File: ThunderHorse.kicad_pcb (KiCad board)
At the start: 6 copper layers, 99.1 x 60 mm, 260 parts, among them J1 JTAG, J10 MOTOR1, J11 SWD1, J12 MOTOR1, J13 SWD1, J14 MOTOR1, J16 UFL, J17 IO1, J18 IO2, J2 HH-16P-CB-TYPE-C, J3 GPS, J4 CAM, J5 GPS, J6 CAM, J7 SWD1, J8 MOTOR1, J9 SWD1, Q1 XRS306D, Q10 XRS306D, Q11 XRS306D, Q12 XRS306D, Q13 SI2312BDS, Q2 XRS306D, Q3 XRS306D, Q4 XRS306D, Q5 XRS306D, Q6 XRS306D, Q7 XRS306D, Q8 XRS306D, Q9 XRS306D, SW1 TS2306A, SW2 TS2306A, U1 BATTERY, U10 STM32G071GBUxN, U11 DRV8300D, U12 STM32G071GBUxN, U13 DRV8300D, U14 STM32G071GBUxN, U15 DRV8300D, U16 TPRT9013-33, U17 ICM-42688-P, U18 BMP280, U19 INA230, U2 TPS63070RNMR, U20 TPRT9013-33, U21 SX1280IMLTRT, U22 AT2401C, U3 TPRT9013-33, U4 TPS2121, U5 RP2354B, U6 W25Q128JVPIQ, U7 USBLC6-2P6, U8 STM32G071GBUxN, U9 DRV8300D, Y1 40MHz, Y2 52MHz/10ppm

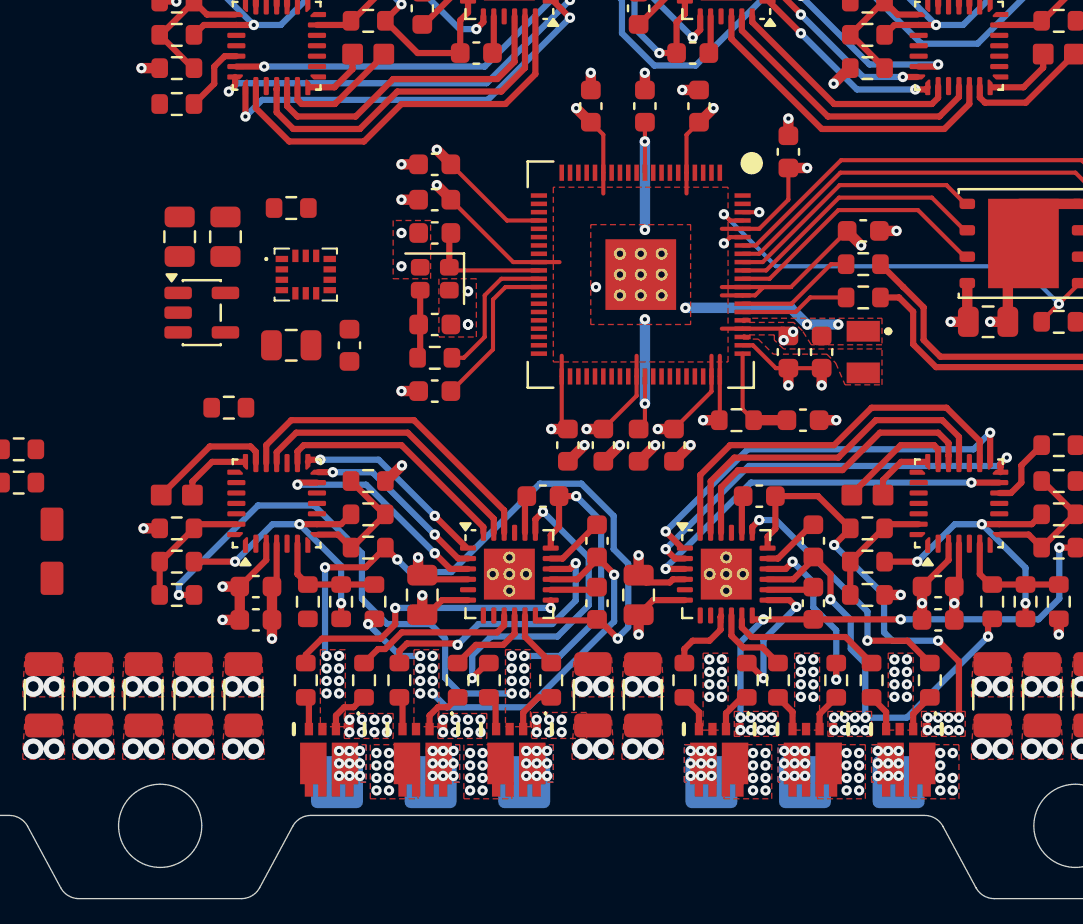
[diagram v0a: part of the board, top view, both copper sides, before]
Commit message: IMU layout
Completed the IMU layout.

TODO:
Continue with the transceiver routing.
Connect each ESC to the MCU.
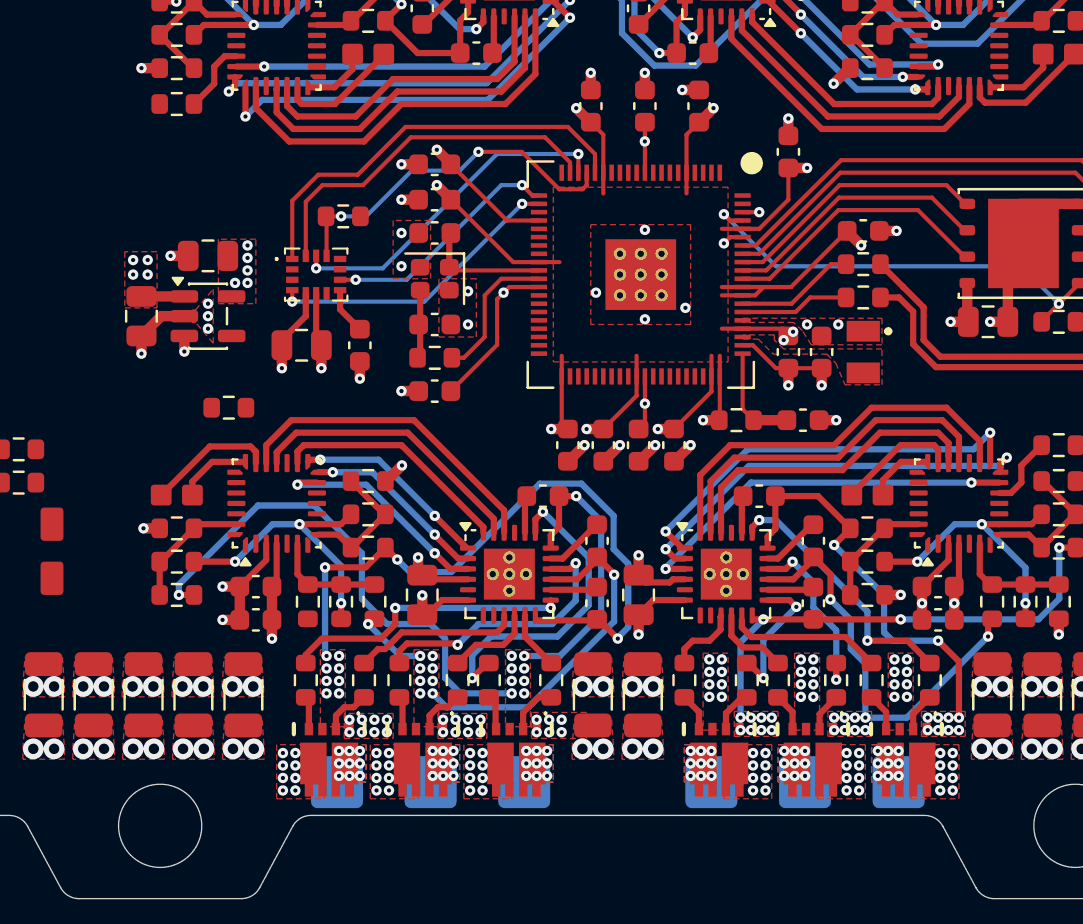
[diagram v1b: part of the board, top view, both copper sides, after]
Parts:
- moved C86 4.24 mm to (117.1, 102.0), turned to -90 degrees
- moved R83 2.53 mm to (126.8, 97.2), turned to 180 degrees
- moved C87 1.24 mm to (120.3, 99.1), turned to 180 degrees
- moved C84 0.50 mm to (124.8, 103.4)
- moved C85 0.50 mm to (127.6, 103.4)
- moved U17 0.50 mm to (125.5, 100.0)
- moved U16 0.34 mm to (120.3, 102.0)
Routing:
- net IMU_MISO: track 0.00 -> 20.3 mm
- net IMU_MOSI: track 0.00 -> 17.6 mm
- net IMU_CS: track 0.00 -> 17.2 mm, vias 0 -> 2
- net IMU_SCLK: track 0.00 -> 16.4 mm, vias 0 -> 2
- net IMU_INT: track 0.00 -> 14.4 mm, vias 0 -> 2
- net IMU_CLK: track 0.00 -> 11.6 mm, vias 0 -> 2
- net GND: track 85.6 -> 94.2 mm, vias 237 -> 243
- net 3V3_IMU: track 0.00 -> 6.34 mm, vias 0 -> 6
- net 1V1: track 29.0 -> 33.3 mm, vias 8 -> 9
- net 5V: track 17.4 -> 20.3 mm, vias 19 -> 24
- net VBAT: vias 160 -> 169
- added copper zone on F.Cu, net 3V3_IMU
- added copper zone on In2.Cu, net 3V3_IMU

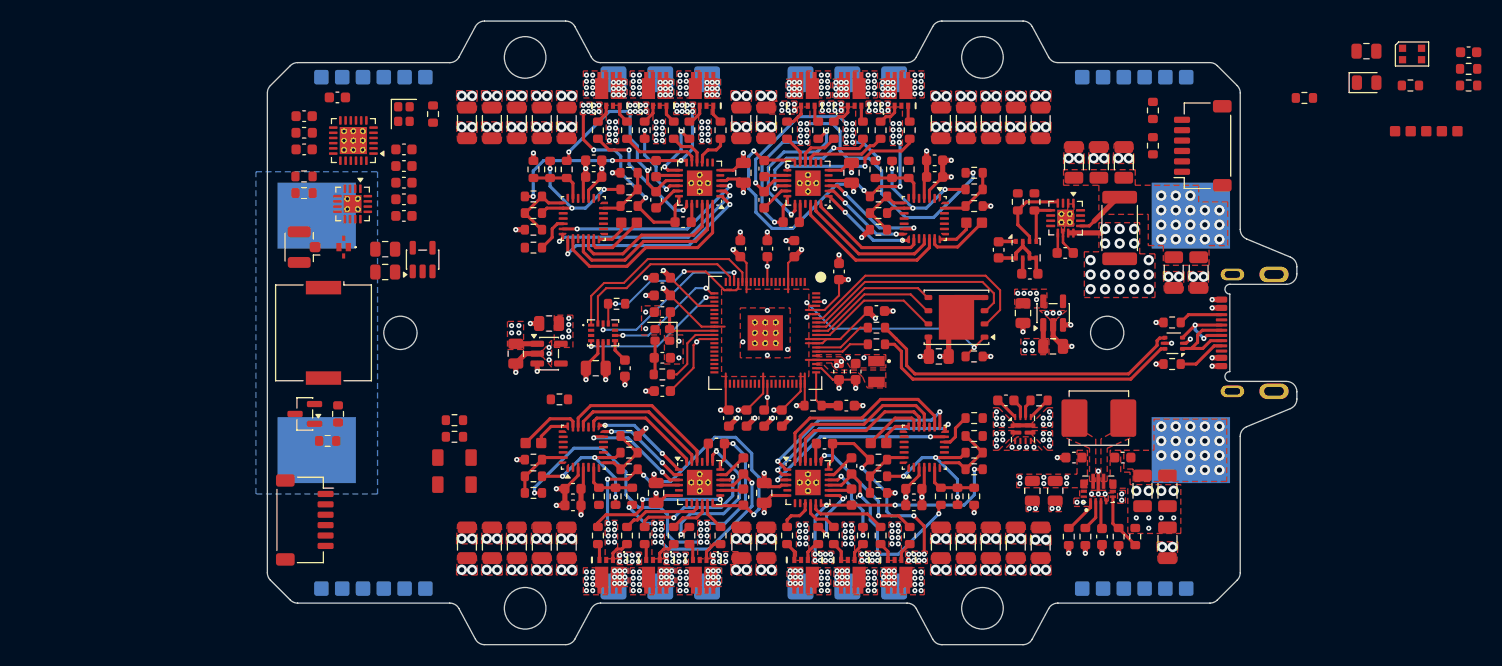
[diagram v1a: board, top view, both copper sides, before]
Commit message: MCU layout
Updated the schematic labels.
Continued the MCU layout.
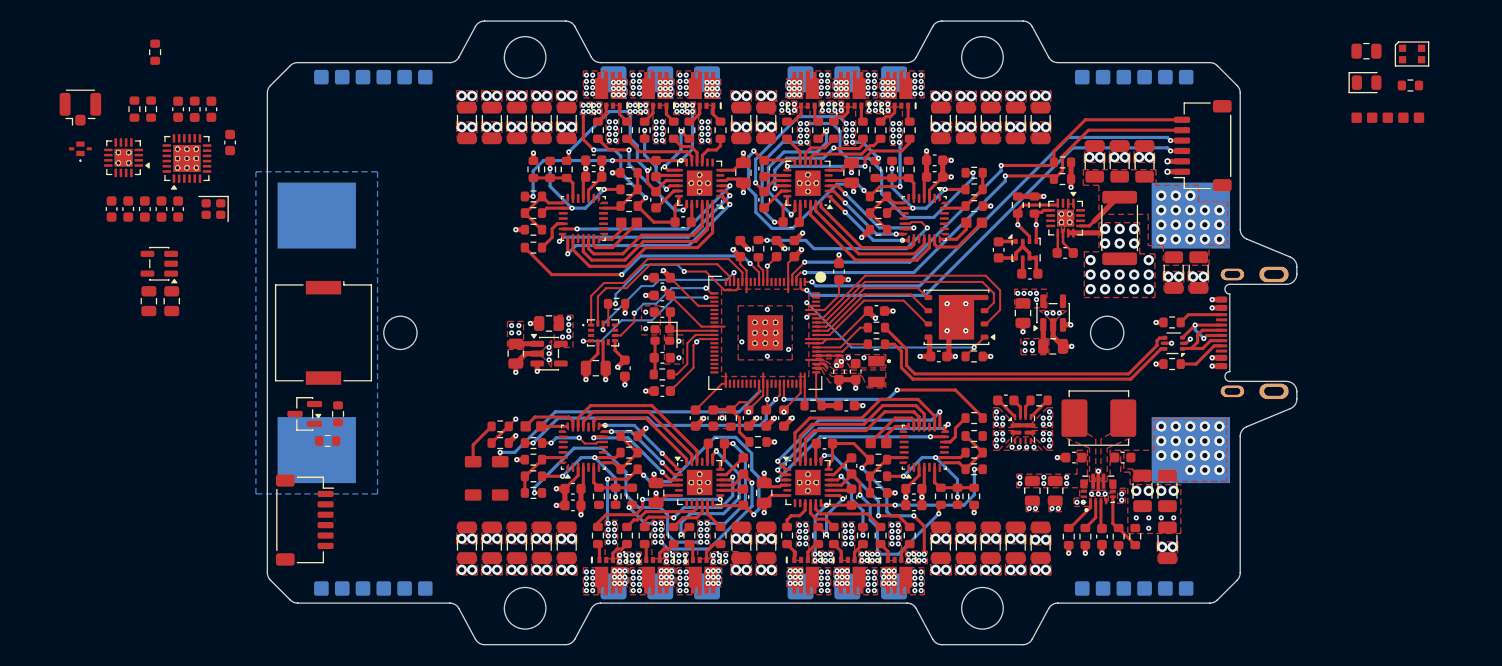
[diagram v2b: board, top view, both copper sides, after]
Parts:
- C35: footprint Capacitor_SMD:C_0805_2012Metric -> Capacitor_SMD:C_0603_1608Metric
- moved C18 80.8 mm to (136.1, 108.2), turned to -90 degrees
- moved R9 77.9 mm to (137.8, 108.2), turned to -90 degrees
- moved R8 77.2 mm to (140.4, 110.5), turned to 0 degrees
- moved R39 54.5 mm to (140.4, 91.9), turned to -90 degrees
- moved C99 28.1 mm to (78.2, 88.1), turned to -90 degrees
- moved R87 27.4 mm to (82.4, 73.0)
- moved FL1 27.0 mm to (75.2, 82.3), turned to 180 degrees
- moved C105 26.5 mm to (79.8, 88.1), turned to -90 degrees
- moved U20 25.3 mm to (82.8, 93.3), turned to 180 degrees
- moved J16 25.3 mm to (75.2, 78.5), turned to 90 degrees
- moved C101 25.1 mm to (81.4, 88.1), turned to -90 degrees
- moved C93 23.7 mm to (83.0, 88.1), turned to -90 degrees
- moved C94 23.3 mm to (81.8, 97.0), turned to -90 degrees
- moved U22 22.5 mm to (79.4, 83.2), turned to 180 degrees
- moved C92 22.5 mm to (84.6, 88.1), turned to -90 degrees
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- renumbered Q6 to Q4, Q4 to Q6, R91 to R85, R92 to R86, R85 to R87, R86 to R88, R87 to R89, R88 to R90, R89 to R91, R90 to R92
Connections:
- R55 pad 2: ESC2 -> ESC3
- U5 pad 11: ESC1 -> ESC2
- U5 pad 12: ESC2 -> ESC1
- U5 pad 13: ESC3 -> unconnected-(U5-GPIO14-Pad13)
- U5 pad 14: ESC4 -> unconnected-(U5-GPIO15-Pad14)
- U5 pad 52: unconnected-(U5-GPIO41/ADC1-Pad52) -> LED1
- U5 pad 53: LED1 -> LED2
- U5 pad 54: LED2 -> ESC3
- U5 pad 55: unconnected-(U5-GPIO44/ADC4-Pad55) -> ESC4
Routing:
- net /MCU/GPS_SCL: track 0.00 -> 45.6 mm, vias 0 -> 2
- net /MCU/GPS_SDA: track 0.00 -> 44.8 mm, vias 0 -> 2
- net /MCU/GPS_RX: track 0.00 -> 43.6 mm, vias 0 -> 2
- net /MCU/GPS_TX: track 0.00 -> 42.5 mm, vias 0 -> 2
- net ESC3: track 0.00 -> 28.7 mm, vias 0 -> 2
- net /MCU/ELRS_BIND: track 0.80 -> 28.3 mm
- net ESC1: track 0.00 -> 25.9 mm, vias 0 -> 2
- net ESC4: track 0.00 -> 22.2 mm, vias 0 -> 2
- net /ESC/ESC2/ESC: track 0.00 -> 20.0 mm, vias 0 -> 2
- net /MCU/VBAT_ADC: track 0.00 -> 9.84 mm
- net /ESC/ESC3/ESC: track 0.00 -> 6.41 mm, vias 0 -> 2
- net /MCU/BOOT_SW: track 0.00 -> 4.14 mm
- net /MCU/QSPI_SS: track 1.02 -> 4.35 mm, vias 1 -> 2
- net 1V1: track 33.3 -> 36.4 mm
- net ESC2: track 0.00 -> 2.57 mm
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
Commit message: Schematic revision
Added an ESP32 C3 for the ELRS receiver.
Updated the protection approach for the board.
Updated the net nodes.
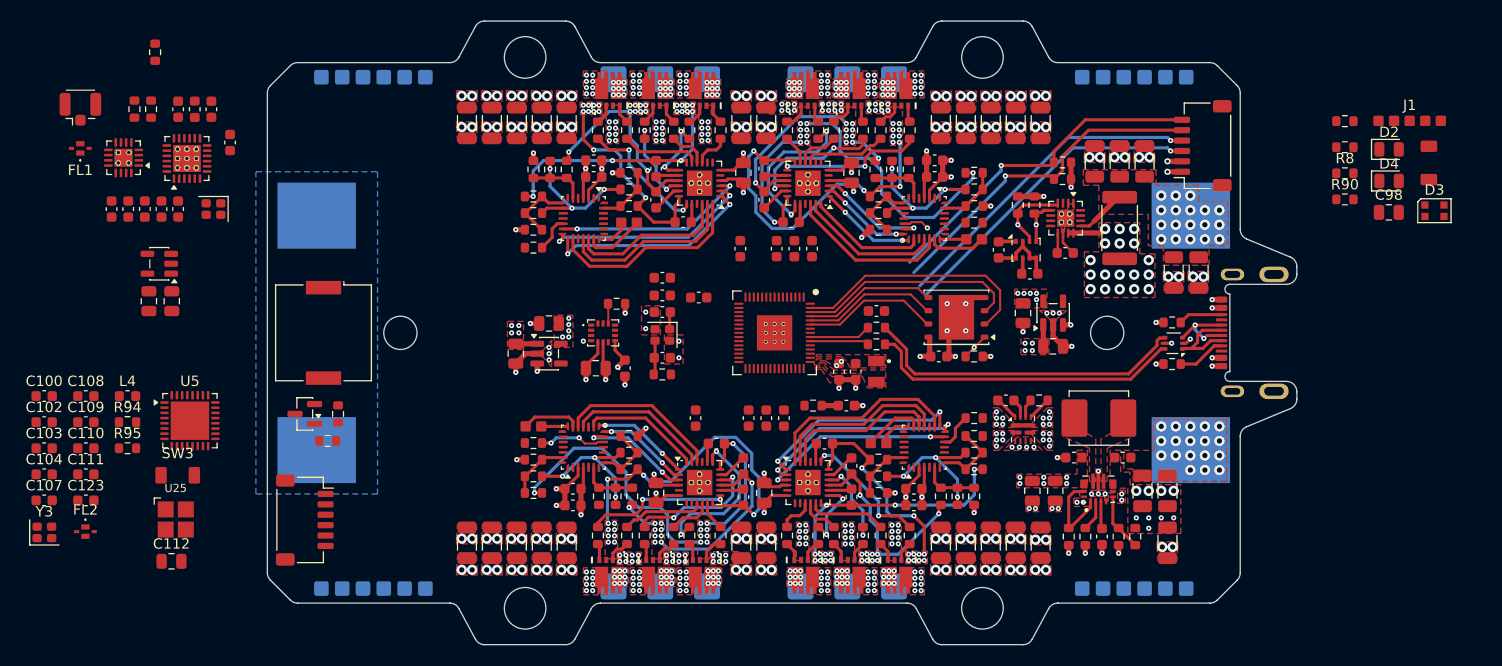
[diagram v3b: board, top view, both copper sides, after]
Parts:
- removed C106: 10u, Capacitor_SMD:C_0805_2012Metric
- removed C18: 100n, Capacitor_SMD:C_0603_1608Metric
- removed D1: WS2812B, Custom_Parts:WS2812B-2020
- removed R9: 10K, Resistor_SMD:R_0603_1608Metric
- removed SW2: TS2306A, Custom_Parts:SW_SMD_3.0x2.0_PUSH
- added C100: 10n, Capacitor_SMD:C_0603_1608Metric, F.Cu at (71.7, 106.1)
- added C102: 1u, Capacitor_SMD:C_0603_1608Metric, F.Cu at (71.7, 108.6)
- added C103: 1u, Capacitor_SMD:C_0603_1608Metric, F.Cu at (71.7, 111.1)
- added C104: 100n, Capacitor_SMD:C_0603_1608Metric, F.Cu at (71.7, 113.6)
- added C107: 15p, Capacitor_SMD:C_0603_1608Metric, F.Cu at (71.7, 116.1)
- added C108: 15p, Capacitor_SMD:C_0603_1608Metric, F.Cu at (75.7, 106.1)
- added C109: 100n, Capacitor_SMD:C_0603_1608Metric, F.Cu at (75.7, 108.6)
- added C110: 1u, Capacitor_SMD:C_0603_1608Metric, F.Cu at (75.7, 111.1)
- added C111: 100n, Capacitor_SMD:C_0603_1608Metric, F.Cu at (75.7, 113.6)
- added C112: 10u, Capacitor_SMD:C_0805_2012Metric, F.Cu at (84.0, 122.0)
- added C123: 1u, Capacitor_SMD:C_0603_1608Metric, F.Cu at (75.7, 116.1)
- added C98: 10u, Capacitor_SMD:C_0805_2012Metric, F.Cu at (201.1, 88.4)
- added D3: WS2812B, Custom_Parts:WS2812B-2020, F.Cu at (205.5, 88.2)
- added D4: GREEN, LED_SMD:LED_0805_2012Metric, F.Cu at (201.1, 85.4)
- added FL2: LFB182G45SG9B740, Custom_Parts:LFB182G45SG9B740, F.Cu at (75.7, 119.1)
- added L4: 2n, Inductor_SMD:L_0603_1608Metric, F.Cu at (79.7, 106.1)
- added R94: 100K, Resistor_SMD:R_0603_1608Metric, F.Cu at (79.7, 108.6)
- added R95: 10K, Resistor_SMD:R_0603_1608Metric, F.Cu at (79.7, 111.1)
- added SW3: TS2306A, Custom_Parts:SW_SMD_3.0x2.0_PUSH, F.Cu at (84.6, 113.7)
- added U23: RP2354A, Custom_Parts:RP2350A_QFN-60_EP_7.75x7.75_Pitch0.4mm, F.Cu at (142.0, 100.0)
- added U25: 0479480001, Custom_Parts:0479480001, F.Cu at (84.4, 118.0)
- added Y3: 40MHz, Crystal:Crystal_SMD_2016-4Pin_2.0x1.6mm, F.Cu at (71.7, 119.2)
- D2: value LED -> BLUE
- R8: value 100K -> 1K
- U5: value RP2354B -> ESP32-C3; footprint Custom_Parts:RP2350B_QFN-80_EP_10.573x10.573_Pitch0.4mm -> Package_DFN_QFN:QFN-32-1EP_5x5mm_P0.5mm_EP3.7x3.7mm
- moved SW1 96.8 mm to (204.9, 83.7)
- moved R6 86.4 mm to (196.9, 79.6)
- moved R7 86.1 mm to (196.9, 82.1)
- moved R8 62.1 mm to (196.9, 84.7)
- moved U5 56.0 mm to (85.8, 108.5), turned to 0 degrees
- moved R39 20.9 mm to (161.2, 89.4), turned to 0 degrees
- moved R90 12.6 mm to (196.9, 87.2)
- moved C34 9.66 mm to (134.7, 96.6)
- moved D2 6.77 mm to (201.1, 82.3)
- moved C22 3.41 mm to (145.6, 91.9)
- moved J1 2.12 mm to (203.1, 79.6), turned to 0 degrees
- moved J9 1.60 mm to (161.2, 91.0)
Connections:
- net /Others/BUZZ_D renamed Net-(BZ1--)
- net /Others/BUZZ_G renamed Net-(Q13-G)
- net /Others/LED1_A renamed Net-(D2-A)
- FL1 pad 1: /Receiver/ANT_FILT -> ANT
- FL1 pad 3: ANT -> Net-(J16-In)
- J16 pad 1: ANT -> Net-(J16-In)
- R8 pad 1: /MCU/VBAT_ADC -> LED_G
- R8 pad 2: VBAT -> Net-(D4-A)
- R87 pad 2: RX_RST -> /Receiver/RST
- R88 pad 1: TX_EN -> /Receiver/TX_EN
- R89 pad 1: RX_EN -> /Receiver/RX_EN
- R90 pad 1: LED1 -> LED_B
- U21 pad 16: RX_MISO -> /Receiver/MISO
- U21 pad 17: RX_MOSI -> /Receiver/MOSI
- U21 pad 18: RX_SCLK -> /Receiver/SCK
- U21 pad 19: RX_CS -> /Receiver/CS
- U21 pad 3: RX_RST -> /Receiver/RST
- U21 pad 7: RX_BUSY -> /Receiver/BUSY
- U21 pad 8: RX_DIO1 -> /Receiver/DIO1
- U21 pad 9: RX_DIO2 -> /Receiver/DIO2
- U22 pad 10: /Receiver/ANT_FILT -> ANT
- U22 pad 5: TX_EN -> /Receiver/TX_EN
- U22 pad 6: RX_EN -> /Receiver/RX_EN
- U5 pad 1: /MCU/GPS_TX -> unconnected-(U5-LNA_IN-Pad1)
- U5 pad 10: 1V1 -> /Receiver/MISO
- U5 pad 11: ESC2 -> 3V3_RX
- U5 pad 12: ESC1 -> /Receiver/SCK
- U5 pad 13: unconnected-(U5-GPIO14-Pad13) -> /Receiver/CS
- U5 pad 14: unconnected-(U5-GPIO15-Pad14) -> LED_RX
- U5 pad 15: 3V3 -> Net-(U5-GPIO9)
- U5 pad 16: IMU_MISO -> unconnected-(U5-GPIO10-Pad16)
- U5 pad 17: IMU_CS -> 3V3_RX
- U5 pad 18: IMU_SCLK -> 3V3_RX
- U5 pad 19: IMU_MOSI -> unconnected-(U5-SPIHD-Pad19)
- U5 pad 2: /MCU/GPS_RX -> /Receiver/VDD
- U5 pad 21: IMU_CLK -> unconnected-(U5-SPICS0-Pad21)
- U5 pad 22: IMU_INT -> unconnected-(U5-SPICLK-Pad22)
- U5 pad 24: 3V3 -> unconnected-(U5-SPIQ-Pad24)
- U5 pad 25: /MCU/CAM_TX -> /Receiver/TX_EN
- U5 pad 26: /MCU/CAM_RX -> /Receiver/RX_EN
- U5 pad 27: /MCU/CAM_SBUS -> ELRS_RX
- U5 pad 28: unconnected-(U5-GPIO27-Pad28) -> ELRS_TX
- U5 pad 29: 3V3 -> /Receiver/XIN
- U5 pad 3: /MCU/GPS_SDA -> /Receiver/VDD
- U5 pad 30: /MCU/XIN -> /Receiver/XOUT
- U5 pad 31: /MCU/XOUT -> 3V3_RX
- U5 pad 32: 1V1 -> 3V3_RX
- U5 pad 33: /MCU/SWCLK -> GND
- U5 pad 4: /MCU/GPS_SCL -> /Receiver/DIO1
- U5 pad 5: 3V3 -> /Receiver/DIO2
- U5 pad 6: GPIO8 -> /Receiver/RST
- U5 pad 7: GPIO9 -> /Receiver/EN
- U5 pad 8: SENS_SDA -> /Receiver/BUSY
- U5 pad 9: SENS_SCL -> /Receiver/MOSI
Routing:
- net 3V3: track 97.7 -> 37.6 mm, vias 26 -> 17
- net 1V1: track 36.4 -> 0.60 mm, vias 9 -> 0
- net ESC3: track 28.7 -> 0.00 mm, vias 2 -> 0
- net /MCU/ELRS_BIND: track 28.3 -> 0.00 mm, vias 1 -> 0
- net ESC1: track 25.9 -> 0.00 mm, vias 2 -> 0
- net ESC4: track 22.2 -> 0.00 mm, vias 2 -> 0
- net IMU_MISO: track 20.3 -> 0.00 mm
- net /MCU/FLASH_SS: track 21.5 -> 2.62 mm, vias 2 -> 1
- net IMU_MOSI: track 17.6 -> 0.00 mm
- net /ESC/ESC2/ESC: track 20.0 -> 2.53 mm, vias 2 -> 1
- net IMU_SCLK: track 16.7 -> 0.00 mm, vias 2 -> 0
- net IMU_CS: track 18.2 -> 1.91 mm, vias 2 -> 0
- net IMU_INT: track 15.1 -> 0.00 mm, vias 2 -> 1
- net /MCU/GPS_RX: track 43.6 -> 30.7 mm, vias 2 -> 1
- net /MCU/GPS_SCL: track 45.6 -> 33.1 mm, vias 2 -> 1
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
